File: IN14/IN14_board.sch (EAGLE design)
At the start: 25 parts, among them T1 BC848, T10 BC848, T11 BC848, T12 BC848, T2 BC848, T3 BC848, T4 BC848, T5 BC848, T6 BC848, T7 BC848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

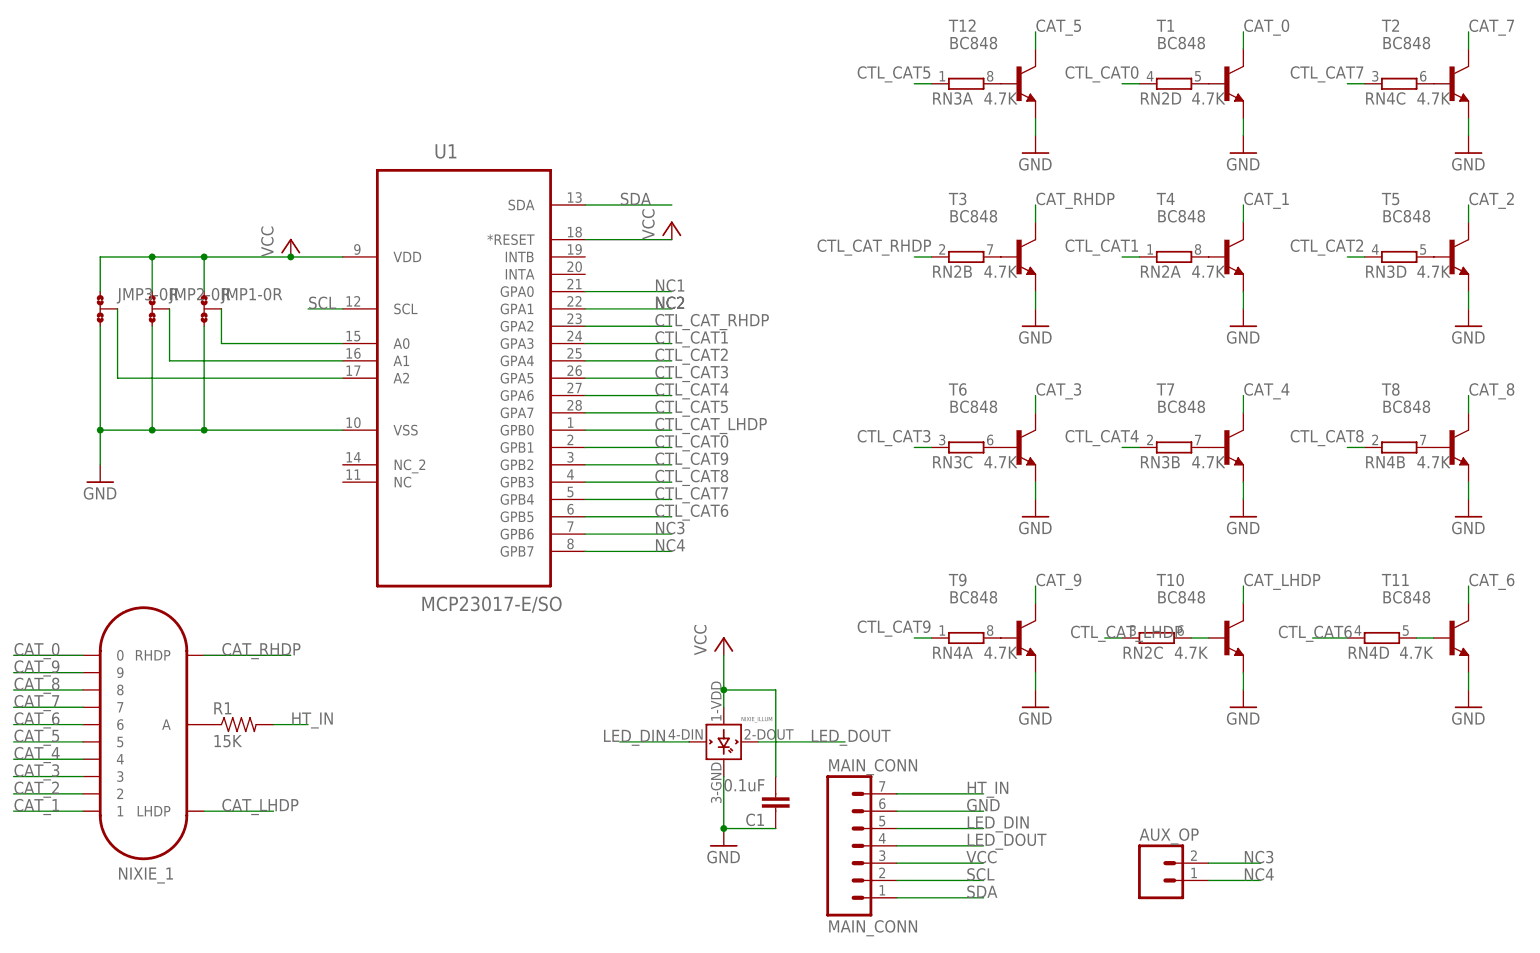
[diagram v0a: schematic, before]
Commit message: Added files via upload
New 'thinner' board - now revision 1.2.  Pincompatible with previous bus-driven designs, but library code will need to be adjusted as the pins are mapped differently for economy of space!
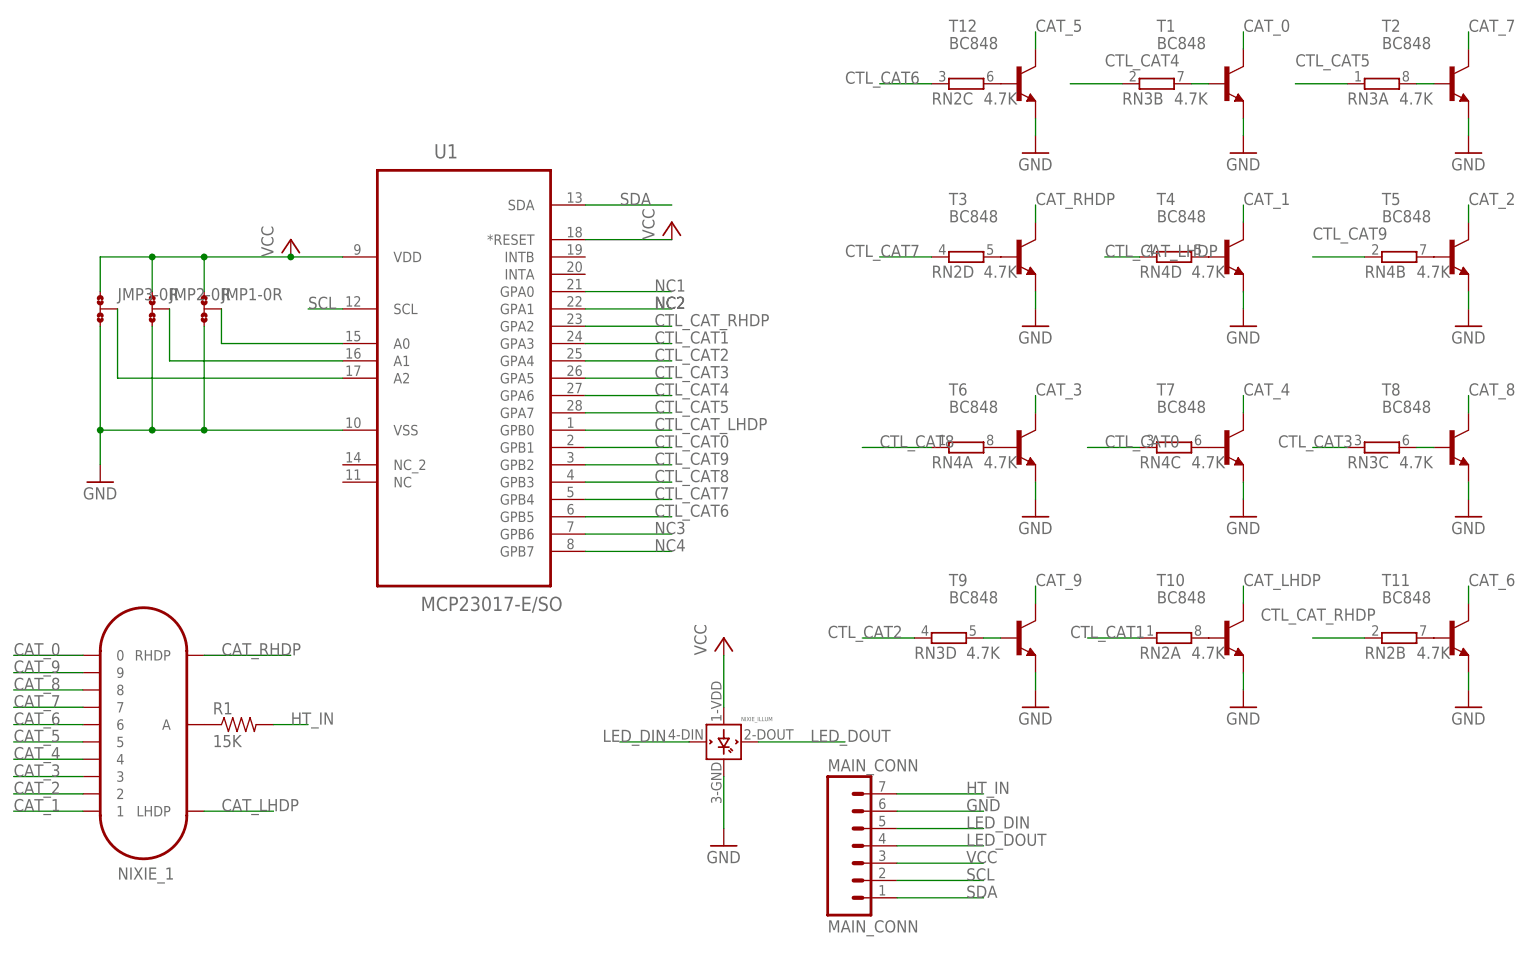
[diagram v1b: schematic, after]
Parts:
- removed AUX_OP: (no value), SparkFun-Connectors:M02LOCK
- removed C1: 0.1uF, SparkFun-Capacitors:0.1UF-25V(+80/-20%)(0603)
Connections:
- removed net N$21: RN2C.2, T10.B
- new net N$16: RN2A.2, T10.B
- net CTL_CAT0: now also RN4C.1; no longer RN2D.1
- net CTL_CAT6: now also RN2C.1; no longer RN4D.1
- net CTL_CAT7: now also RN2D.1; no longer RN4C.1
- net CTL_CAT8: now also RN4A.1; no longer RN4B.1
- net CTL_CAT9: now also RN4B.1; no longer RN4A.1
- net CTL_CAT_LHDP: now also RN4D.1; no longer RN2C.1
- net GND: no longer C1.1
- net N$1: now also T2.B; no longer T12.B
- net N$10: now also RN4A.2, T6.B; no longer RN4D.2, T11.B
- net N$11: now also T9.B; no longer T5.B
- net N$12: now also T5.B; no longer T8.B
- net N$13: now also RN4C.2, T7.B; no longer RN3C.2, T6.B
- net N$14: now also RN2C.2, T12.B; no longer RN4A.2, T9.B
- net N$15: now also RN2B.2, T11.B; no longer RN3B.2, T7.B
- net N$3: now also RN3B.2; no longer RN2D.2
- net N$5: now also RN3C.2, T8.B; no longer RN4C.2, T2.B
- net N$7: now also RN2D.2; no longer RN2B.2
- net N$9: now also RN4D.2; no longer RN2A.2
- net NC3: no longer AUX_OP.2
- net NC4: no longer AUX_OP.1
- net VCC: no longer C1.2
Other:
- moved on the sheet: RN2A, RN2B, RN2C, RN2D, RN3A, RN3B, RN3C, RN3D, RN4A, RN4B, RN4C, RN4D
